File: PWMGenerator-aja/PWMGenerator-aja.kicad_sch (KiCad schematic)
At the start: 30 parts, among them J1 Conn_01x03_Pin, Q1 NPN, Q2 NPN, Q3 PNP, Q4 PNP, SW1 SW_SPST, U1 LM7805_TO220, U2 LM339

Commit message: Rev 0.4.  Release version of A solution. Updated PCB Project A notes.
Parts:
- Q4: footprint (none) -> Package_TO_SOT_THT:TO-92_Inline
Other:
- moved on the sheet: C1, C2, C3, D1, D2, D3, D4, D5, D6, F1, J1, Q1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

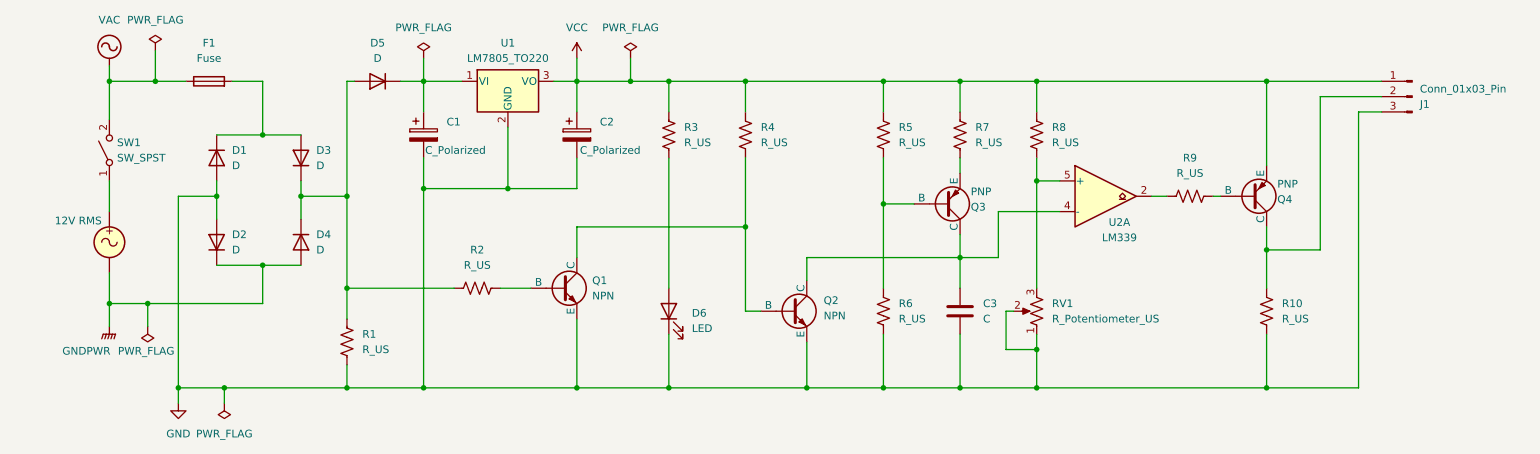
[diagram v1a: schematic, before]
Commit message: Resistors and diodes annotated.
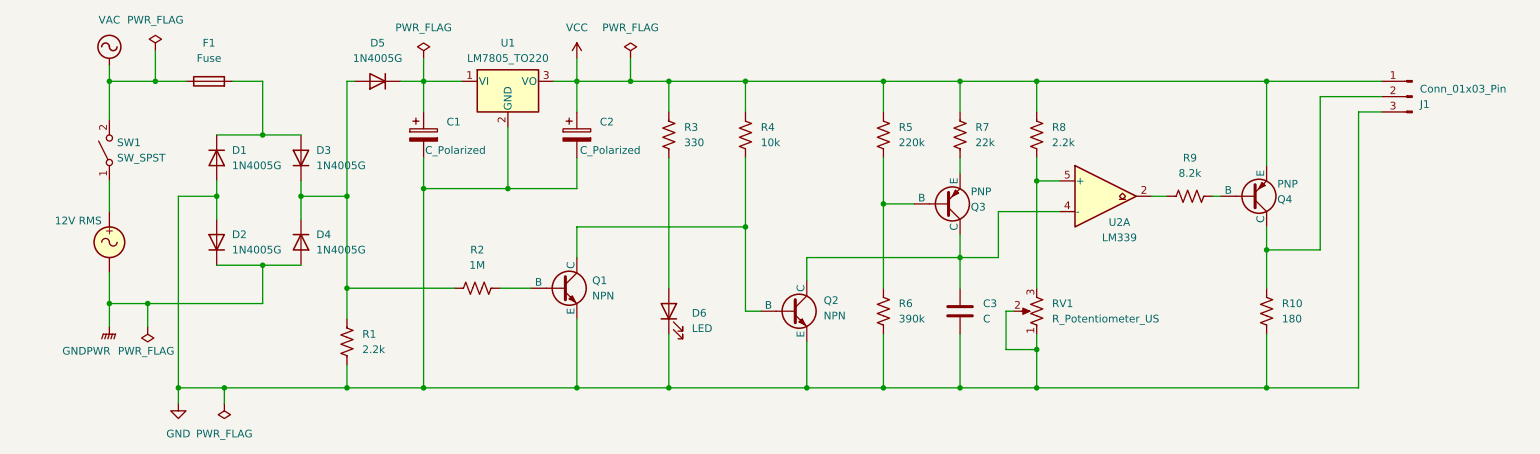
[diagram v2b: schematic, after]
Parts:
- D1: value D -> 1N4005G; footprint (none) -> Diode_SMD:D_0805_2012Metric; symbol Device:D -> Diode:1N4005
- D2, D3, D4, D5: value D -> 1N4005G; footprint (none) -> Diode_SMD:D_0805_2012Metric
- R1, R8: value R_US -> 2.2k; footprint (none) -> Resistor_SMD:R_0805_2012Metric
- R10: value R_US -> 180; footprint (none) -> Resistor_SMD:R_0805_2012Metric
- R2: value R_US -> 1M; footprint (none) -> Resistor_SMD:R_0805_2012Metric
- R3: value R_US -> 330; footprint (none) -> Resistor_SMD:R_0805_2012Metric
- R4: value R_US -> 10k; footprint (none) -> Resistor_SMD:R_0805_2012Metric
- R5: value R_US -> 220k; footprint (none) -> Resistor_SMD:R_0805_2012Metric
- R6: value R_US -> 390k; footprint (none) -> Resistor_SMD:R_0805_2012Metric
- R7: value R_US -> 22k; footprint (none) -> Resistor_SMD:R_0805_2012Metric
- R9: value R_US -> 8.2k; footprint (none) -> Resistor_SMD:R_0805_2012Metric
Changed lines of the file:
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@@
 		(title "CMPE2150 PWM Generator - aja")
 		(date "2024-12-03")
-		(rev "0.4")
+		(rev "0.5")
 		(company "NAIT CNT")
 		(comment 1 "Author: AJ Armstrong")
@@
 	)
 	(symbol
-		(lib_id "Device:D")
+		(lib_id "Diode:1N4005")
 		(at 46.99 76.2 270)
 		(unit 1)
@@
 		(on_board yes)
 		(dnp no)
-		(fields_autoplaced yes)
 		(property "Reference" "D1"
 			(at 49.53 74.9299 90)
@@
 			)
 		)
-		(property "Value" "D"
+		(property "Value" "1N4005G"
 			(at 49.53 77.4699 90)
 			(effects
@@
 			)
 		)
-		(property "Footprint" ""
-			(at 46.99 76.2 0)
+		(property "Footprint" "Diode_SMD:D_0805_2012Metric"
+			(at 42.545 76.2 0)
 			(effects
 				(font
@@
 			)
 		)
-		(property "Datasheet" "~"
+		(property "Datasheet" "http://www.vishay.com/docs/88503/1n4001.pdf"
 			(at 46.99 76.2 0)
 			(effects
@@
 			)
 		)
-		(property "Description" "Diode"
+		(property "Description" "600V 1A General Purpose Rectifier Diode, DO-41"
 			(at 46.99 76.2 0)
 			(effects
@@
 			)
 		)
-		(property "Value" "R_US"
+		(property "Value" "2.2k"
 			(at 71.12 107.9499 0)
 			(effects
@@
 			)
 		)
-		(property "Footprint" ""
+		(property "Footprint" "Resistor_SMD:R_0805_2012Metric"
 			(at 69.596 106.934 90)
 			(effects
@@
 			)
 		)
-		(property "Value" "R_US"
+		(property "Value" "330"
 			(at 124.46 73.6599 0)
 			(effects
@@
 			)
 		)
-		(property "Footprint" ""
+		(property "Footprint" "Resistor_SMD:R_0805_2012Metric"
 			(at 120.904 72.136 90)
 			(effects
@@
 			)
 		)
-		(property "Value" "R_US"
+		(property "Value" "22k"
 			(at 172.72 73.6599 0)
 			(effects
@@
 			)
 		)
-		(property "Footprint" ""
+		(property "Footprint" "Resistor_SMD:R_0805_2012Metric"
 			(at 169.164 72.136 90)
 			(effects
@@
 			)
 		)
-		(property "Value" "R_US"
+		(property "Value" "180"
 			(at 223.52 102.8699 0)
 			(effects
@@
 			)
 		)
-		(property "Footprint" ""
+		(property "Footprint" "Resistor_SMD:R_0805_2012Metric"
 			(at 221.996 101.854 90)
 			(effects
@@
 			)
 		)
-		(property "Value" "R_US"
+		(property "Value" "10k"
 			(at 137.16 73.6599 0)
 			(effects
@@
 			)
 		)
-		(property "Footprint" ""
+		(property "Footprint" "Resistor_SMD:R_0805_2012Metric"
 			(at 133.604 72.136 90)
 			(effects
@@
 			)
 		)
-		(property "Value" "R_US"
+		(property "Value" "2.2k"
 			(at 185.42 73.6599 0)
 			(effects
@@
 			)
 		)
-		(property "Footprint" ""
+		(property "Footprint" "Resistor_SMD:R_0805_2012Metric"
 			(at 181.864 72.136 90)
 			(effects
@@
 			)
 		)
-		(property "Value" "D"
+		(property "Value" "1N4005G"
 			(at 63.5 91.4399 90)
 			(effects
@@
 			)
 		)
-		(property "Footprint" ""
+		(property "Footprint" "Diode_SMD:D_0805_2012Metric"
 			(at 60.96 90.17 0)
 			(effects
@@
 			)
 		)
-		(property "Datasheet" "~"
+		(property "Datasheet" "http://www.vishay.com/docs/88503/1n4001.pdf"
 			(at 60.96 90.17 0)
 			(effects
@@
 			)
 		)
-		(property "Value" "R_US"
+		(property "Value" "1M"
 			(at 90.17 93.98 90)
 			(effects
@@
 			)
 		)
-		(property "Footprint" ""
+		(property "Footprint" "Resistor_SMD:R_0805_2012Metric"
 			(at 90.424 96.774 90)
 			(effects
@@
 			)
 		)
-		(property "Value" "D"
+		(property "Value" "1N4005G"
 			(at 63.5 77.4699 90)
 			(effects
@@
 			)
 		)
-		(property "Footprint" ""
+		(property "Footprint" "Diode_SMD:D_0805_2012Metric"
 			(at 60.96 76.2 0)
 			(effects
@@
 			)
 		)
-		(property "Datasheet" "~"
+		(property "Datasheet" "http://www.vishay.com/docs/88503/1n4001.pdf"
 			(at 60.96 76.2 0)
 			(effects
@@
 			)
 		)
-		(property "Value" "R_US"
+		(property "Value" "390k"
 			(at 160.02 102.8699 0)
 			(effects
@@
 			)
 		)
-		(property "Footprint" ""
+		(property "Footprint" "Resistor_SMD:R_0805_2012Metric"
 			(at 156.464 101.346 90)
 			(effects
@@
 			)
 		)
-		(property "Value" "R_US"
+		(property "Value" "8.2k"
 			(at 208.28 78.74 90)
 			(effects
@@
 			)
 		)
-		(property "Footprint" ""
+		(property "Footprint" "Resistor_SMD:R_0805_2012Metric"
 			(at 208.026 83.566 90)
 			(effects
@@
 			)
 		)
-		(property "Value" "D"
+		(property "Value" "1N4005G"
 			(at 73.66 59.69 0)
 			(effects
@@
 			)
 		)
-		(property "Footprint" ""
+		(property "Footprint" "Diode_SMD:D_0805_2012Metric"
 			(at 73.66 63.5 0)
 			(effects
@@
 			)
 		)
-		(property "Datasheet" "~"
+		(property "Datasheet" "http://www.vishay.com/docs/88503/1n4001.pdf"
 			(at 73.66 63.5 0)
 			(effects
@@
 		(on_board yes)
 		(dnp no)
-		(fields_autoplaced yes)
 		(property "Reference" "D2"
 			(at 49.53 88.8999 90)
@@
 			)
 		)
-		(property "Value" "D"
+		(property "Value" "1N4005G"
 			(at 49.53 91.4399 90)
 			(effects
@@
 			)
 		)
-		(property "Footprint" ""
+		(property "Footprint" "Diode_SMD:D_0805_2012Metric"
 			(at 46.99 90.17 0)
 			(effects
@@
 			)
 		)
-		(property "Datasheet" "~"
+		(property "Datasheet" "http://www.vishay.com/docs/88503/1n4001.pdf"
 			(at 46.99 90.17 0)
 			(effects
@@
 			)
 		)
-		(property "Value" "R_US"
+		(property "Value" "220k"
 			(at 160.02 73.6599 0)
 			(effects
@@
 			)
 		)
-		(property "Footprint" ""
+		(property "Footprint" "Resistor_SMD:R_0805_2012Metric"
 			(at 156.464 72.136 90)
 			(effects

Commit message: Well along in annotations.
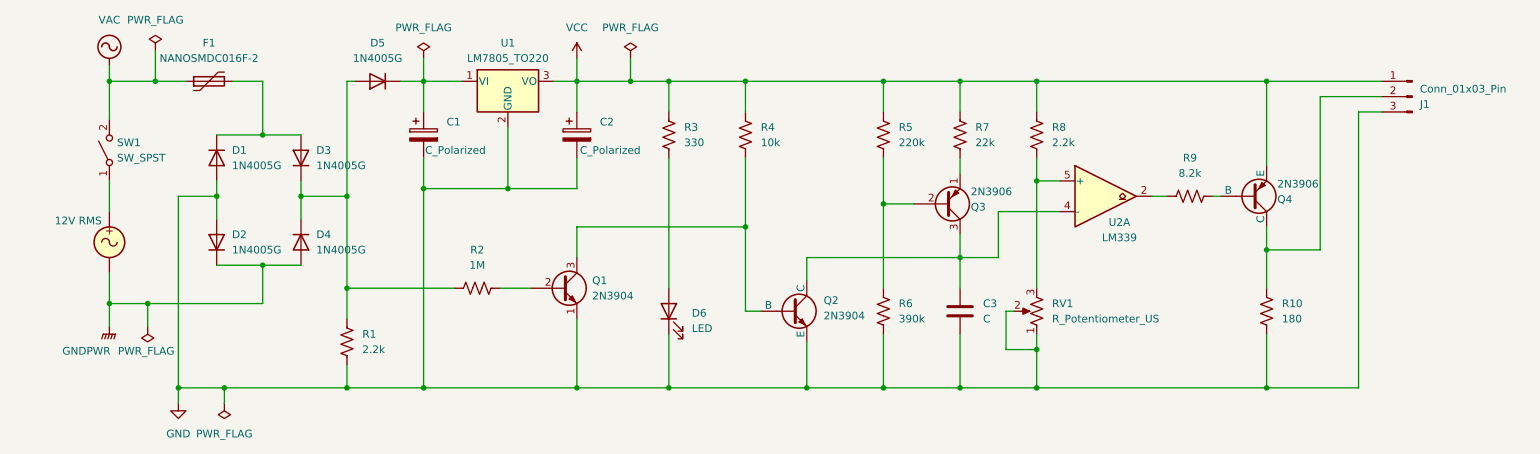
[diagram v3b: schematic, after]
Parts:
- F1: value Fuse -> NANOSMDC016F-2; footprint (none) -> local:RESC3115X65N; symbol Device:Fuse -> Device:Polyfuse
- Q1: value NPN -> 2N3904; footprint (none) -> Package_TO_SOT_SMD:SOT-23; symbol Simulation_SPICE:NPN -> Transistor_BJT:2N3904
- Q2: value NPN -> 2N3904; footprint (none) -> Package_TO_SOT_SMD:SOT-23
- Q3: value PNP -> 2N3906; footprint (none) -> Package_TO_SOT_THT:TO-92_Inline; symbol Simulation_SPICE:PNP -> Transistor_BJT:2N3906
- Q4: value PNP -> 2N3906; footprint Package_TO_SOT_THT:TO-92_Inline -> Package_TO_SOT_SMD:SOT-23
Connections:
- net GND: now also Q1.1 (E); no longer Q1.3 (E)
- net at R7.1: now also Q3.1 (E); no longer Q3.3 (E)
- net at Q2.2 (B), R4.1: now also Q1.3 (C); no longer Q1.1 (C)
- net at C3.1, Q2.1 (C), U2.4 (-): now also Q3.3 (C); no longer Q3.1 (C)
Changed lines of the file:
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@@
 			)
 		)
-		(property "Value" "PNP"
+		(property "Value" "2N3906"
 			(at 222.758 80.518 0)
 			(effects
@@
 			)
 		)
-		(property "Footprint" "Package_TO_SOT_THT:TO-92_Inline"
+		(property "Footprint" "Package_TO_SOT_SMD:SOT-23"
 			(at 254 82.55 0)
 			(effects
@@
 			)
 		)
-		(property "Datasheet" "https://ngspice.sourceforge.io/docs/ngspice-html-manual/manual.xhtml#cha_BJTs"
+		(property "Datasheet" "https://www.onsemi.com/pub/Collateral/2N3906-D.PDF"
 			(at 254 82.55 0)
 			(effects
@@
 	)
 	(symbol
-		(lib_id "Device:Fuse")
+		(lib_id "Device:Polyfuse")
 		(at 45.72 63.5 90)
 		(unit 1)
@@
 			)
 		)
-		(property "Value" "Fuse"
+		(property "Value" "NANOSMDC016F-2"
 			(at 45.72 59.69 90)
 			(effects
@@
 			)
 		)
-		(property "Footprint" ""
-			(at 45.72 65.278 90)
-			(effects
-				(font
-					(size 1.27 1.27)
-				)
-				(hide yes)
-			)
-		)
-		(property "Datasheet" "~"
+		(property "Footprint" "local:RESC3115X65N"
+			(at 50.8 62.23 0)
+			(effects
+				(font
+					(size 1.27 1.27)
+				)
+				(justify left)
+				(hide yes)
+			)
+		)
+		(property "Datasheet" "https://www.littelfuse.com/assetdocs/littelfuse-ptc-nanosmdc-datasheet?assetguid=2f577573-06ff-4a40-bed7-97598401ae57"
 			(at 45.72 63.5 0)
 			(effects
@@
 			)
 		)
-		(property "Description" "Fuse"
+		(property "Description" "Resettable fuse, polymeric positive temperature coefficient"
 			(at 45.72 63.5 0)
 			(effects
@@
 			)
 		)
-		(property "Value" "NPN"
+		(property "Value" "2N3904"
 			(at 147.574 102.362 0)
 			(effects
@@
 			)
 		)
-		(property "Footprint" ""
+		(property "Footprint" "Package_TO_SOT_SMD:SOT-23"
 			(at 205.74 101.6 0)
 			(effects
@@
 			)
 		)
-		(property "Datasheet" "https://ngspice.sourceforge.io/docs/ngspice-html-manual/manual.xhtml#cha_BJTs"
+		(property "Datasheet" "https://www.onsemi.com/pub/Collateral/2N3903-D.PDF"
 			(at 205.74 101.6 0)
 			(effects
@@
 	)
 	(symbol
-		(lib_id "Simulation_SPICE:NPN")
+		(lib_id "Transistor_BJT:2N3904")
 		(at 104.14 97.79 0)
 		(unit 1)
@@
 			)
 		)
-		(property "Value" "NPN"
+		(property "Value" "2N3904"
 			(at 109.22 99.0599 0)
 			(effects
@@
 			)
 		)
-		(property "Footprint" ""
-			(at 167.64 97.79 0)
-			(effects
-				(font
-					(size 1.27 1.27)
-				)
-				(hide yes)
-			)
-		)
-		(property "Datasheet" "https://ngspice.sourceforge.io/docs/ngspice-html-manual/manual.xhtml#cha_BJTs"
-			(at 167.64 97.79 0)
-			(effects
-				(font
-					(size 1.27 1.27)
-				)
-				(hide yes)
-			)
-		)
-		(property "Description" "Bipolar transistor symbol for simulation only, substrate tied to the emitter"
+		(property "Footprint" "Package_TO_SOT_SMD:SOT-23"
+			(at 109.22 99.695 0)
+			(effects
+				(font
+					(size 1.27 1.27)
+					(italic yes)
+				)
+				(justify left)
+				(hide yes)
+			)
+		)
+		(property "Datasheet" "https://www.onsemi.com/pub/Collateral/2N3903-D.PDF"
+			(at 104.14 97.79 0)
+			(effects
+				(font
+					(size 1.27 1.27)
+				)
+				(justify left)
+				(hide yes)
+			)
+		)
+		(property "Description" "0.2A Ic, 40V Vce, Small Signal NPN Transistor, TO-92"
 			(at 104.14 97.79 0)
 			(effects
@@
 	)
 	(symbol
-		(lib_id "Simulation_SPICE:PNP")
+		(lib_id "Transistor_BJT:2N3906")
 		(at 167.64 83.82 0)
 		(mirror x)
@@
 			)
 		)
-		(property "Value" "PNP"
+		(property "Value" "2N3906"
 			(at 171.958 81.788 0)
 			(effects
@@
 			)
 		)
-		(property "Footprint" ""
-			(at 203.2 83.82 0)
-			(effects
-				(font
-					(size 1.27 1.27)
-				)
-				(hide yes)
-			)
-		)
-		(property "Datasheet" "https://ngspice.sourceforge.io/docs/ngspice-html-manual/manual.xhtml#cha_BJTs"
-			(at 203.2 83.82 0)
-			(effects
-				(font
-					(size 1.27 1.27)
-				)
-				(hide yes)
-			)
-		)
-		(property "Description" "Bipolar transistor symbol for simulation only, substrate tied to the emitter"
+		(property "Footprint" "Package_TO_SOT_THT:TO-92_Inline"
+			(at 172.72 81.915 0)
+			(effects
+				(font
+					(size 1.27 1.27)
+					(italic yes)
+				)
+				(justify left)
+				(hide yes)
+			)
+		)
+		(property "Datasheet" "https://www.onsemi.com/pub/Collateral/2N3906-D.PDF"
 			(at 167.64 83.82 0)
 			(effects
+				(font
+					(size 1.27 1.27)
+				)
+				(justify left)
+				(hide yes)
+			)
+		)
+		(property "Description" "-0.2A Ic, -40V Vce, Small Signal PNP Transistor, TO-92"
+			(at 167.64 83.82 0)
+			(effects

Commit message: Getting there on PCB Project B.
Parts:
- C1: value C_Polarized -> 220uF
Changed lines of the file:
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@@
 			)
 		)
-		(property "Value" "C_Polarized"
+		(property "Value" "220uF"
 			(at 81.534 74.93 0)
 			(effects

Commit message: Done everything but three parts.
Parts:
- C1: footprint (none) -> Capacitor_THT:CP_Radial_D10.0mm_P5.00mm
- C2: value C_Polarized -> 10uF; footprint (none) -> Capacitor_THT:CP_Radial_D5.0mm_P2.00mm
- C3: value C -> 0.1uF; footprint (none) -> Capacitor_SMD:C_0805_2012Metric
- J1: footprint (none) -> Connector_PinHeader_2.54mm:PinHeader_1x03_P2.54mm_Horizontal
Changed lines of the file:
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@@
 			)
 		)
-		(property "Value" "C"
+		(property "Value" "0.1uF"
 			(at 173.99 102.8699 0)
 			(effects
@@
 			)
 		)
-		(property "Footprint" ""
+		(property "Footprint" "Capacitor_SMD:C_0805_2012Metric"
 			(at 171.1452 105.41 0)
 			(effects
@@
 			)
 		)
-		(property "Value" "C_Polarized"
+		(property "Value" "10uF"
 			(at 107.188 74.93 0)
 			(effects
@@
 			)
 		)
-		(property "Footprint" ""
+		(property "Footprint" "Capacitor_THT:CP_Radial_D5.0mm_P2.00mm"
 			(at 107.6452 76.2 0)
 			(effects
@@
 			)
 		)
-		(property "Datasheet" "~"
+		(property "Datasheet" "https://www.vishay.com/docs/28402/142rhs.pdf"
 			(at 106.68 72.39 0)
 			(effects
@@
 			)
 		)
-		(property "Footprint" ""
+		(property "Footprint" "Connector_PinHeader_2.54mm:PinHeader_1x03_P2.54mm_Horizontal"
 			(at 245.11 66.04 0)
 			(effects
@@
 			)
 		)
-		(property "Footprint" ""
+		(property "Footprint" "Capacitor_THT:CP_Radial_D10.0mm_P5.00mm"
 			(at 82.2452 76.2 0)
 			(effects
@@
 			)
 		)
-		(property "Datasheet" "~"
+		(property "Datasheet" "https://www.vishay.com/docs/28321/136rvi.pdf"
 			(at 81.28 72.39 0)
 			(effects

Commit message: All but barrel jack
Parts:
- D6: value LED -> LED Green; footprint (none) -> LED_THT:LED_D5.0mm_Green
- RV1: value R_Potentiometer_US -> 5k; footprint (none) -> Potentiometer_THT:Potentiometer_ACP_CA9-V10_Vertical
- SW1: footprint (none) -> Button_Switch_SMD:SW_DIP_SPSTx01_Slide_Omron_A6S-110x_W8.9mm_P2.54mm
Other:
- moved on the sheet: F1
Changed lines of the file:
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@@
 		(title "CMPE2150 PWM Generator - aja")
 		(date "2024-12-03")
-		(rev "0.5")
+		(rev "0.6")
 		(company "NAIT CNT")
 		(comment 1 "Author: AJ Armstrong")
@@
 	(wire
 		(pts
-			(xy 36.83 63.5) (xy 41.91 63.5)
+			(xy 36.83 63.5) (xy 43.18 63.5)
 		)
 		(stroke
@@
 	(wire
 		(pts
-			(xy 54.61 63.5) (xy 49.53 63.5)
+			(xy 54.61 63.5) (xy 50.8 63.5)
 		)
 		(stroke
@@
 		)
 		(property "Value" "2N3906"
-			(at 222.758 80.518 0)
+			(at 223.52 73.406 90)
 			(effects
 				(font
@@
 		(on_board yes)
 		(dnp no)
-		(fields_autoplaced yes)
 		(property "Reference" "C3"
-			(at 173.99 100.3299 0)
+			(at 170.942 104.394 0)
 			(effects
 				(font
@@
 		)
 		(property "Value" "0.1uF"
-			(at 173.99 102.8699 0)
+			(at 170.942 106.934 0)
 			(effects
 				(font
@@
 		(on_board yes)
 		(dnp no)
-		(fields_autoplaced yes)
 		(property "Reference" "D4"
-			(at 63.5 88.8999 90)
+			(at 61.468 87.63 90)
 			(effects
 				(font
@@
 		)
 		(property "Value" "1N4005G"
-			(at 63.5 91.4399 90)
+			(at 63.754 89.916 0)
 			(effects
 				(font
@@
 	(symbol
 		(lib_id "Device:Polyfuse")
-		(at 45.72 63.5 90)
+		(at 46.99 63.5 90)
 		(unit 1)
 		(exclude_from_sim no)
@@
 		(fields_autoplaced yes)
 		(property "Reference" "F1"
-			(at 45.72 57.15 90)
+			(at 46.99 57.15 90)
 			(effects
 				(font
@@
 		)
 		(property "Value" "NANOSMDC016F-2"
-			(at 45.72 59.69 90)
+			(at 46.99 59.69 90)
 			(effects
 				(font
@@
 		)
 		(property "Footprint" "local:RESC3115X65N"
-			(at 50.8 62.23 0)
+			(at 52.07 62.23 0)
 			(effects
 				(font
@@
 		)
 		(property "Datasheet" "https://www.littelfuse.com/assetdocs/littelfuse-ptc-nanosmdc-datasheet?assetguid=2f577573-06ff-4a40-bed7-97598401ae57"
-			(at 45.72 63.5 0)
+			(at 46.99 63.5 0)
 			(effects
 				(font
@@
 		)
 		(property "Description" "Resettable fuse, polymeric positive temperature coefficient"
-			(at 45.72 63.5 0)
+			(at 46.99 63.5 0)
 			(effects
 				(font
@@
 			)
 		)
-		(property "Value" "LED"
+		(property "Value" "LED Green"
 			(at 125.73 104.4574 90)
 			(effects
@@
 			)
 		)
-		(property "Footprint" ""
+		(property "Footprint" "LED_THT:LED_D5.0mm_Green"
 			(at 121.92 101.6 0)
 			(effects
@@
 		(on_board yes)
 		(dnp no)
-		(fields_autoplaced yes)
 		(property "Reference" "D3"
-			(at 63.5 74.9299 90)
+			(at 60.96 79.248 90)
 			(effects
 				(font
@@
 		)
 		(property "Value" "1N4005G"
-			(at 63.5 77.4699 90)
+			(at 64.008 68.58 0)
 			(effects
 				(font
@@
 			)
 		)
-		(property "Value" "R_Potentiometer_US"
+		(property "Value" "5k"
 			(at 185.42 102.8699 0)
 			(effects
@@
 			)
 		)
-		(property "Footprint" ""
+		(property "Footprint" "Potentiometer_THT:Potentiometer_ACP_CA9-V10_Vertical"
 			(at 182.88 101.6 0)
 			(effects
@@
 			)
 		)
-		(property "Footprint" ""
+		(property "Footprint" "Button_Switch_SMD:SW_DIP_SPSTx01_Slide_Omron_A6S-110x_W8.9mm_P2.54mm"
 			(at 29.21 74.93 0)
 			(effects
@@
 			)
 		)
-		(property "Datasheet" "~"
+		(property "Datasheet" "https://omronfs.omron.com/en_US/ecb/products/pdf/en-a6sn.pdf"
 			(at 29.21 74.93 0)
 			(effects
